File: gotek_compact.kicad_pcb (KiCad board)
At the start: 4 copper layers, 55 x 42 mm, 45 parts, among them CN1 POWER_IN, CN2 USB, CN3 Floppy 34, J1 Sound, J2 USB_Prog, J3 OLED+SER, J4 Encoder, Q1 MMBT3904, U1 STM32F105RBT6, U2 74LCX07, U3 AP2112K-3.3, X1 8MHz

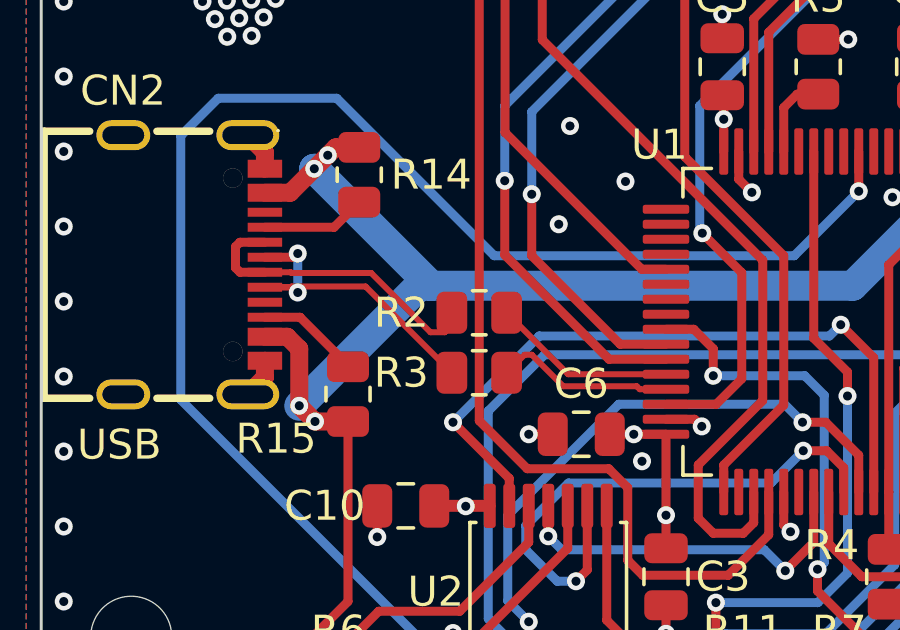
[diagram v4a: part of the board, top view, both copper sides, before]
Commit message: USB differential routing fix
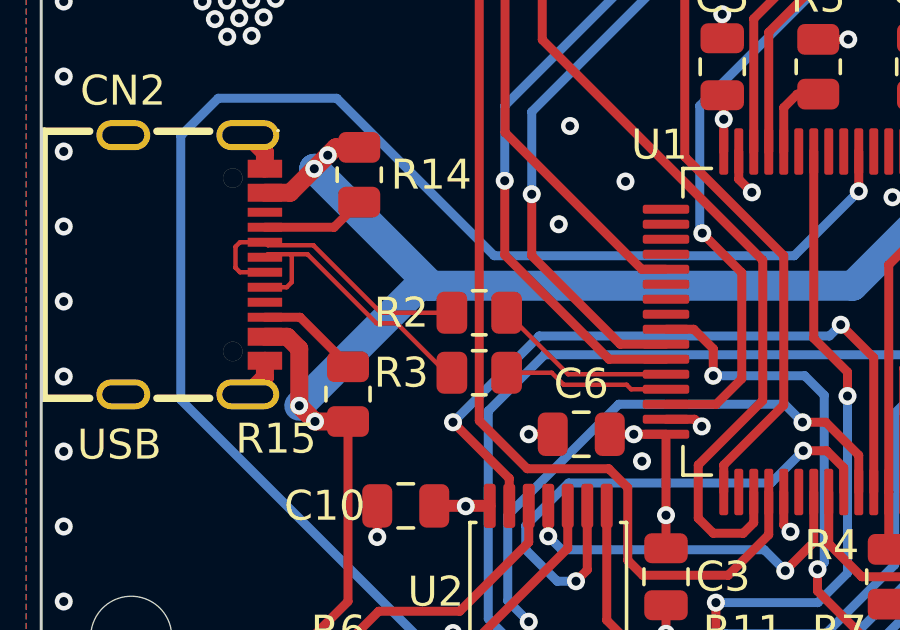
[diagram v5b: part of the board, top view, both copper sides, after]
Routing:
- net USB_D+: track 11.0 -> 9.81 mm, vias 2 -> 0
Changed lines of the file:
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@@
 	)
 	(segment
-		(start 59.95 39.75)
-		(end 59.85 39.65)
-		(width 0.2)
+		(start 57.017525 39.2)
+		(end 55.5125 39.2)
+		(width 0.15)
 		(layer "F.Cu")
 		(net "USB_ST_D+")
 	)
 	(segment
+		(start 59.662499 39.75)
+		(end 59.512499 39.6)
+		(width 0.15)
+		(layer "F.Cu")
+		(net "USB_ST_D+")
+	)
+	(segment
+		(start 59.512499 39.6)
+		(end 57.417525 39.6)
+		(width 0.15)
+		(layer "F.Cu")
+		(net "USB_ST_D+")
+	)
+	(segment
 		(start 60.825 39.75)
-		(end 59.95 39.75)
-		(width 0.2)
+		(end 59.662499 39.75)
+		(width 0.15)
 		(layer "F.Cu")
 		(net "USB_ST_D+")
 	)
 	(segment
-		(start 59.85 39.65)
-		(end 57.4 39.65)
-		(width 0.2)
+		(start 57.417525 39.6)
+		(end 57.017525 39.2)
+		(width 0.15)
 		(layer "F.Cu")
 		(net "USB_ST_D+")
 	)
 	(segment
-		(start 56.35 38.6)
-		(end 56.1125 38.6)
-		(width 0.2)
-		(layer "F.Cu")
-		(net "USB_ST_D+")
-	)
-	(segment
-		(start 57.4 39.65)
-		(end 56.35 38.6)
-		(width 0.2)
-		(layer "F.Cu")
-		(net "USB_ST_D+")
-	)
-	(segment
-		(start 56.1125 38.6)
-		(end 55.5125 39.2)
-		(width 0.2)
-		(layer "F.Cu")
-		(net "USB_ST_D+")
-	)
-	(segment
-		(start 48.342501 36.325)
-		(end 50.8125 36.325)
-		(width 0.2)
+		(start 47.455 36.35)
+		(end 48.18 36.35)
+		(width 0.15)
 		(layer "F.Cu")
 		(net "USB_D+")
 	)
 	(segment
-		(start 48.375 36.35)
-		(end 48.55 36.525)
-		(width 0.2)
+		(start 47.555 35.25)
+		(end 47.455 35.35)
+		(width 0.15)
 		(layer "F.Cu")
 		(net "USB_D+")
 	)
 	(segment
-		(start 48.425 35.35)
-		(end 48.55 35.225)
-		(width 0.3)
+		(start 48.35 35.25)
+		(end 47.555 35.25)
+		(width 0.15)
 		(layer "F.Cu")
 		(net "USB_D+")
 	)
 	(segment
-		(start 48.317501 36.35)
-		(end 48.342501 36.325)
-		(width 0.2)
+		(start 53.5 39.2)
+		(end 51.85 37.55)
+		(width 0.15)
 		(layer "F.Cu")
 		(net "USB_D+")
 	)
 	(segment
-		(start 50.8125 36.325)
-		(end 53.6875 39.2)
-		(width 0.2)
+		(start 48.875 35.25)
+		(end 48.35 35.25)
+		(width 0.15)
 		(layer "F.Cu")
 		(net "USB_D+")
 	)
 	(segment
-		(start 47.455 35.35)
-		(end 48.425 35.35)
-		(width 0.3)
+		(start 51.175 37.55)
+		(end 48.875 35.25)
+		(width 0.15)
 		(layer "F.Cu")
 		(net "USB_D+")
 	)
 	(segment
-		(start 47.455 36.35)
-		(end 48.317501 36.35)
-		(width 0.2)
+		(start 48.35 36.18)
+		(end 48.35 35.25)
+		(width 0.15)
 		(layer "F.Cu")
 		(net "USB_D+")
 	)
 	(segment
-		(start 47.455 36.35)
-		(end 48.375 36.35)
-		(width 0.2)
+		(start 53.6875 39.2)
+		(end 53.5 39.2)
+		(width 0.15)
 		(layer "F.Cu")
 		(net "USB_D+")
 	)
-	(via
-		(at 48.55 36.525)
-		(size 0.6)
-		(drill 0.3)
-		(layers "F.Cu" "B.Cu")
+	(segment
+		(start 51.85 37.55)
+		(end 51.175 37.55)
+		(width 0.15)
+		(layer "F.Cu")
 		(net "USB_D+")
 	)
-	(via
-		(at 48.55 35.225)
-		(size 0.6)
-		(drill 0.3)
-		(layers "F.Cu" "B.Cu")
-		(net "USB_D+")
-	)
-	(segment
-		(start 48.55 35.225)
-		(end 48.55 36.525)
-		(width 0.3)
-		(layer "B.Cu")
+	(segment
+		(start 48.18 36.35)
+		(end 48.35 36.18)
+		(width 0.15)
+		(layer "F.Cu")
 		(net "USB_D+")
 	)
@@
 	)
 	(segment
+		(start 57.5625 39.25)
+		(end 55.5125 37.2)
+		(width 0.15)
+		(layer "F.Cu")
+		(net "USB_ST_D-")
+	)
+	(segment
 		(start 60.825 39.25)
 		(end 57.5625 39.25)
-		(width 0.2)
-		(layer "F.Cu")
-		(net "USB_ST_D-")
-	)
-	(segment
-		(start 57.5625 39.25)
-		(end 55.5125 37.2)
-		(width 0.2)
+		(width 0.15)
 		(layer "F.Cu")
 		(net "USB_ST_D-")
@@
 	)
 	(segment
-		(start 52.973896 37.85)
-		(end 53.45 37.85)
-		(width 0.2)
-		(layer "F.Cu")
-		(net "USB_D-")
-	)
-	(segment
-		(start 53.6875 37.6125)
-		(end 53.6875 37.2)
-		(width 0.2)
+		(start 47.555 34.95)
+		(end 47.455 34.85)
+		(width 0.15)
 		(layer "F.Cu")
 		(net "USB_D-")
@@
 		(start 46.475 35)
 		(end 46.475 35.7)
-		(width 0.3)
-		(layer "F.Cu")
-		(net "USB_D-")
-	)
-	(segment
-		(start 53.45 37.85)
-		(end 53.6875 37.6125)
-		(width 0.2)
+		(width 0.15)
 		(layer "F.Cu")
 		(net "USB_D-")
@@
 		(start 47.455 34.85)
 		(end 46.625 34.85)
-		(width 0.3)
+		(width 0.15)
 		(layer "F.Cu")
 		(net "USB_D-")
@@
 		(start 46.625 35.85)
 		(end 47.455 35.85)
-		(width 0.3)
+		(width 0.15)
 		(layer "F.Cu")
 		(net "USB_D-")
 	)
 	(segment
-		(start 50.998896 35.875)
-		(end 52.973896 37.85)
-		(width 0.2)
+		(start 51.319974 37.2)
+		(end 49.069974 34.95)
+		(width 0.15)
 		(layer "F.Cu")
 		(net "USB_D-")
 	)
 	(segment
-		(start 47.455 35.85)
-		(end 48.317501 35.85)
-		(width 0.2)
-		(layer "F.Cu")
-		(net "USB_D-")
-	)
-	(segment
-		(start 48.317501 35.85)
-		(end 48.342501 35.875)
-		(width 0.2)
-		(layer "F.Cu")
-		(net "USB_D-")
-	)
-	(segment
-		(start 48.342501 35.875)
-		(end 50.998896 35.875)
-		(width 0.2)
+		(start 49.069974 34.95)
+		(end 47.555 34.95)
+		(width 0.15)
 		(layer "F.Cu")
 		(net "USB_D-")
@@
 		(start 46.625 34.85)
 		(end 46.475 35)
-		(width 0.3)
+		(width 0.15)
 		(layer "F.Cu")
 		(net "USB_D-")
@@
 		(start 46.475 35.7)
 		(end 46.625 35.85)
-		(width 0.3)
+		(width 0.15)
 		(layer "F.Cu")
 		(net "USB_D-")
+	)
+	(segment
+		(start 53.6875 37.2)
+		(end 51.319974 37.2)
+		(width 0.15)
+		(layer "F.Cu")
+		(net "USB_D-")
